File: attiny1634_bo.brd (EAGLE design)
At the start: 49.5 x 22.2 mm, 11 parts, among them J1 AVR_SPI_PRG_6NS, Y1 12MHz

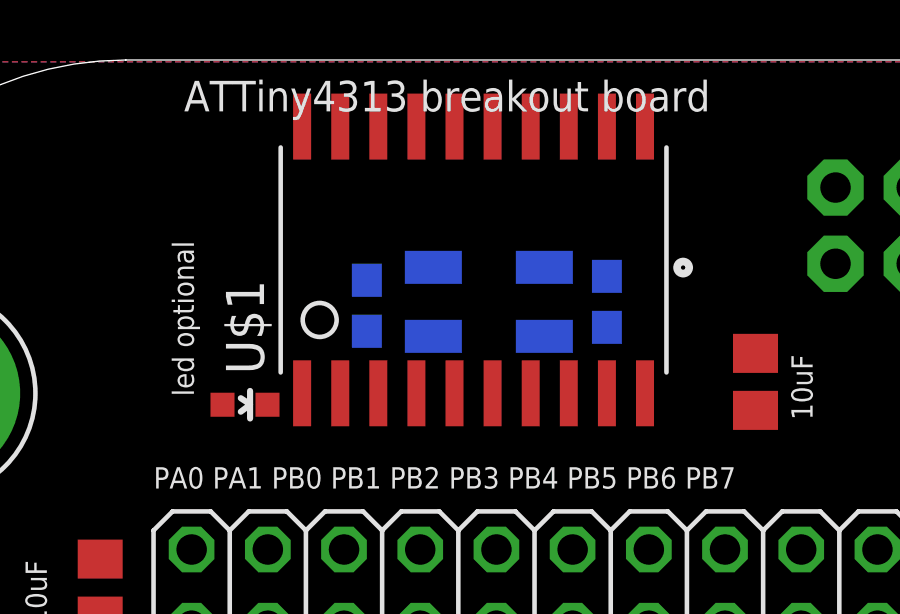
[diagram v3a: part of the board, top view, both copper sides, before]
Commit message: minor fixes to the lib, connected programming signals and xtal
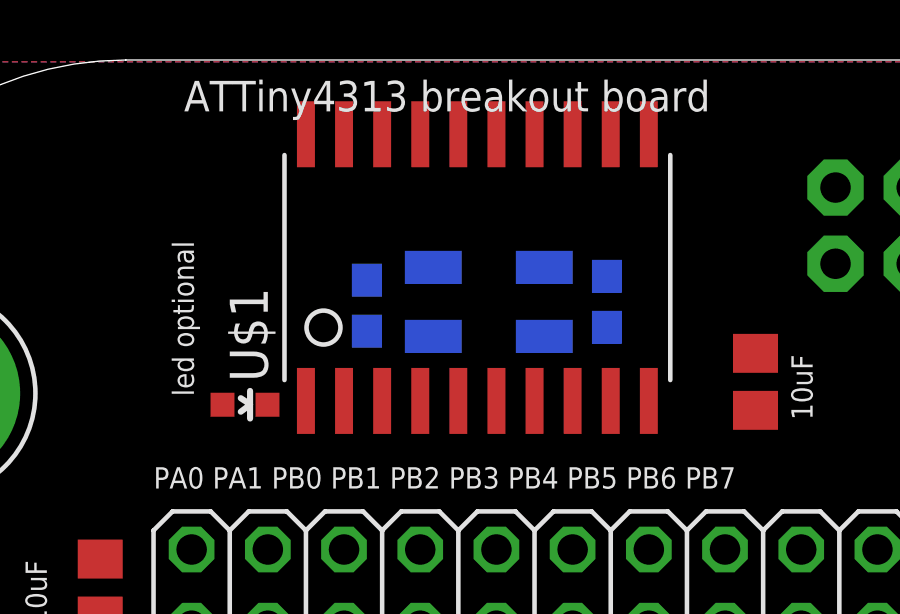
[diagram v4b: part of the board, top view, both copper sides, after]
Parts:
- moved U$1 8.02 mm to (19.3, 15.2)
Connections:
- removed net N$11: CX0.2, Y1.3
- removed net N$3: J1.5
- removed net N$4: J1.4
- removed net N$7: J1.3
- removed net N$9: CX1.2, Y1.1
- removed net PB6/MISO: J1.1
- removed net PD6: LED1.C
- removed net VCC: U$1.11
- new net PB0/MOSI/TX0/ADC5: J1.4, U$1.1
- new net PB1/ADC6: LED1.C, U$1.20
- new net PB2/ADC7/TX1: J1.1, U$1.19
- new net PC1/SCL/ADC10: J1.3, U$1.16
- new net PC3/-RESET: J1.5, U$1.14
- new net PC4/XTAL2: CX0.2, U$1.13, Y1.3
- new net PC5/XTAL1: CX1.2, U$1.12, Y1.1
- net +5V: now also U$1.11
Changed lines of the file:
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@@
 <text x="34.29" y="10.16" size="0.7112" layer="25" font="vector" rot="R90">10uF</text>
 <text x="29.845" y="17.145" size="0.7112" layer="26" rot="MR0">12pF caps for xtal</text>
-<circle x="29.972" y="15.24" radius="0.127" width="0.4064" layer="25"/>
 </plain>
 <attributes>
@@
 <attribute name="VALUE" x="37.719" y="9.017" size="1.27" layer="27" rot="R180"/>
 </element>
-<element name="U$1" library="attiny1634" package="SOIC20" value="ATTINY1634" x="14.097" y="9.144"/>
+<element name="U$1" library="attiny1634" package="SOIC20" value="ATTINY1634" x="19.304" y="15.24"/>
 </elements>
 <signals>
@@
 <contactref element="JP1" pad="18"/>
 <contactref element="U$1" pad="10"/>
+<contactref element="U$1" pad="10"/>
 <wire x1="35.052" y1="15.367" x2="45.466" y2="10.795" width="0" layer="19" extent="1-1"/>
 <wire x1="32.385" y1="12.38" x2="35.052" y2="15.367" width="0" layer="19" extent="1-1"/>
-<wire x1="28.702" y1="11.049" x2="32.385" y2="12.38" width="0" layer="19" extent="1-1"/>
-<wire x1="27.432" y1="14.947" x2="28.702" y2="11.049" width="0" layer="19" extent="1-16"/>
+<wire x1="28.829" y1="10.795" x2="32.385" y2="12.38" width="0" layer="19" extent="1-1"/>
+<wire x1="27.432" y1="14.947" x2="28.829" y2="10.795" width="0" layer="19" extent="1-16"/>
 <wire x1="19.431" y1="13.12" x2="27.432" y2="14.947" width="0" layer="19" extent="16-16"/>
 <wire x1="16.129" y1="3.302" x2="19.431" y2="13.12" width="0" layer="19" extent="16-16"/>
@@
 <contactref element="JP1" pad="2"/>
 <contactref element="JP1" pad="20"/>
+<contactref element="U$1" pad="11"/>
 <wire x1="32.385" y1="10.48" x2="40.132" y2="15.367" width="0" layer="19" extent="1-1"/>
 <wire x1="36.449" y1="3.302" x2="32.385" y2="10.48" width="0" layer="19" extent="1-1"/>
-<wire x1="14.617" y1="10.668" x2="32.385" y2="10.48" width="0" layer="19" extent="1-1"/>
+<wire x1="28.829" y1="19.685" x2="32.385" y2="10.48" width="0" layer="19" extent="1-1"/>
+<wire x1="14.617" y1="10.668" x2="28.829" y2="19.685" width="0" layer="19" extent="1-1"/>
 <wire x1="13.589" y1="3.302" x2="14.617" y2="10.668" width="0" layer="19" extent="1-1"/>
 <wire x1="10.541" y1="3.622" x2="13.589" y2="3.302" width="0" layer="19" extent="1-1"/>
 </signal>
-<signal name="PB6/MISO">
+<signal name="PB1/ADC6">
+<contactref element="LED1" pad="C"/>
+<contactref element="U$1" pad="20"/>
+<wire x1="16.117" y1="10.668" x2="17.399" y2="19.685" width="0" layer="19" extent="1-1"/>
+</signal>
+<signal name="PB0/MOSI/TX0/ADC5">
+<contactref element="J1" pad="4"/>
+<contactref element="U$1" pad="1"/>
+<wire x1="17.399" y1="10.795" x2="37.592" y2="15.367" width="0" layer="19" extent="1-1"/>
+</signal>
+<signal name="PC1/SCL/ADC10">
+<contactref element="U$1" pad="16"/>
+<contactref element="J1" pad="3"/>
+<wire x1="22.479" y1="19.685" x2="37.592" y2="17.907" width="0" layer="19" extent="1-1"/>
+</signal>
+<signal name="PB2/ADC7/TX1">
+<contactref element="U$1" pad="19"/>
 <contactref element="J1" pad="1"/>
-</signal>
-<signal name="PD6">
-<contactref element="LED1" pad="C"/>
-</signal>
-<signal name="N$3">
+<wire x1="18.669" y1="19.685" x2="40.132" y2="17.907" width="0" layer="19" extent="1-1"/>
+</signal>
+<signal name="PC3/-RESET">
+<contactref element="U$1" pad="14"/>
 <contactref element="J1" pad="5"/>
-</signal>
-<signal name="N$4">
-<contactref element="J1" pad="4"/>
-</signal>
-<signal name="N$7">
-<contactref element="J1" pad="3"/>
-</signal>
-<signal name="N$9">
+<wire x1="25.019" y1="19.685" x2="35.052" y2="17.907" width="0" layer="19" extent="1-1"/>
+</signal>
+<signal name="PC5/XTAL1">
+<contactref element="U$1" pad="12"/>
 <contactref element="CX1" pad="2"/>
 <contactref element="Y1" pad="1"/>
+<wire x1="27.432" y1="13.247" x2="27.559" y2="19.685" width="0" layer="19" extent="1-16"/>
 <wire x1="25.345" y1="12.947" x2="27.432" y2="13.247" width="0" layer="19" extent="16-16"/>
 </signal>
-<signal name="N$11">
+<signal name="PC4/XTAL2">
+<contactref element="U$1" pad="13"/>
 <contactref element="CX0" pad="2"/>
 <contactref element="Y1" pad="3"/>
+<wire x1="21.645" y1="15.247" x2="26.289" y2="19.685" width="0" layer="19" extent="1-16"/>
 <wire x1="19.431" y1="14.82" x2="21.645" y2="15.247" width="0" layer="19" extent="16-16"/>
 </signal>
-<signal name="VCC">
-<contactref element="U$1" pad="11"/>
-</signal>
 </signals>

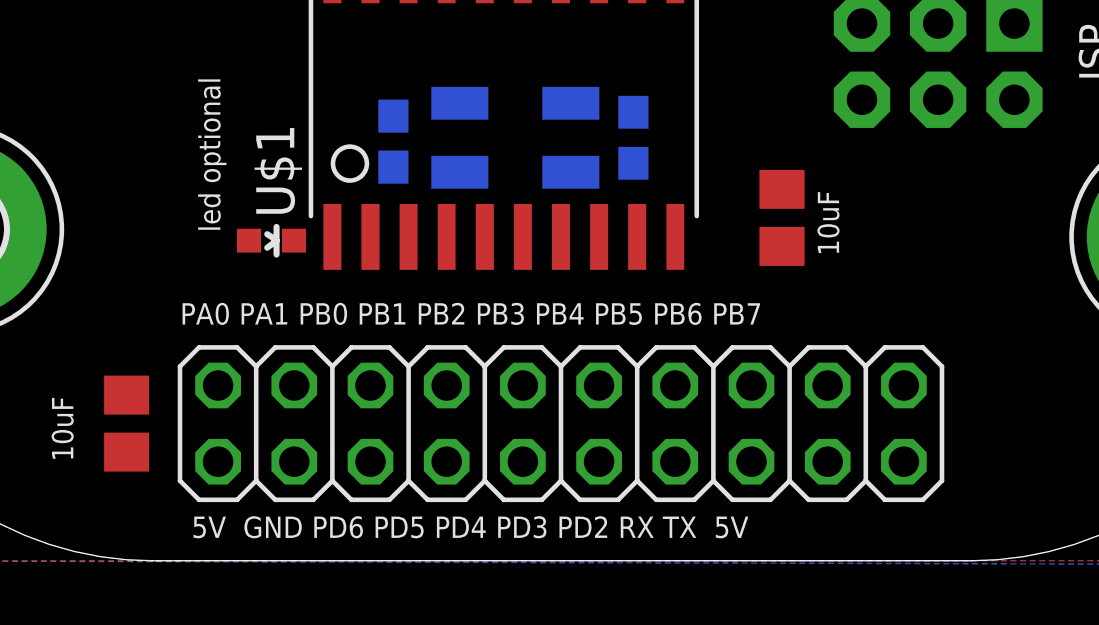
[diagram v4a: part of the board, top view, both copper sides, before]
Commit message: connected portA
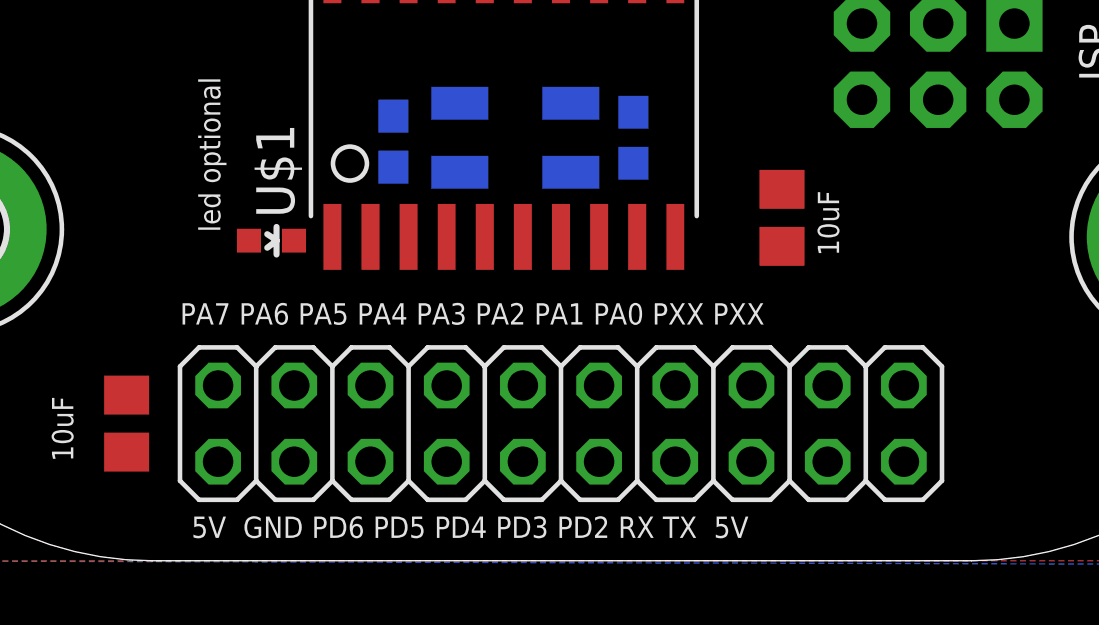
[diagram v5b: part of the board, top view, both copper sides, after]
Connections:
- new net PA0: JP1.5, U$1.9
- new net PA1: JP1.7, U$1.8
- new net PA2: JP1.9, U$1.7
- new net PA3: JP1.11, U$1.6
- new net PA4: JP1.13, U$1.5
- new net PA5: JP1.15, U$1.4
- new net PA6: JP1.17, U$1.3
- new net PA7: JP1.19, U$1.2
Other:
- board text added: "PA7 PA6 PA5 PA4 PA3 PA2 PA1 PA0 PXX PXX"
- board text added: "PXX PXX PA0 PA1 PA2 PA3 PA4 PA5 PA6 PA7"
- board text removed: "PA0 PA1 PB0 PB1 PB2 PB3 PB4 PB5 PB6 PB7"
- board text removed: "PB7 PB6 PB5 PB4 PB3 PB2 PB1 PB0 PA1 PA0"
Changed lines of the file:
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@@
 <text x="13.335" y="20.447" size="1.016" layer="25" font="vector">ATTiny4313 breakout board</text>
 <text x="42.291" y="17.907" size="1.016" layer="25" font="vector" rot="R270">ISP</text>
-<text x="37.338" y="7.874" size="0.7112" layer="26" font="vector" rot="MR0">PB7 PB6 PB5 PB4 PB3 PB2 PB1 PB0 PA1 PA0</text>
+<text x="37.338" y="7.874" size="0.7112" layer="26" font="vector" rot="MR0">PXX PXX PA0 PA1 PA2 PA3 PA4 PA5 PA6 PA7</text>
 <text x="37.211" y="0.635" size="0.762" layer="26" font="vector" rot="MR0">5V RX TX PD2 PD3 PD4 PD5 PD6 GND 5V</text>
-<text x="12.319" y="7.874" size="0.7112" layer="25" font="vector">PA0 PA1 PB0 PB1 PB2 PB3 PB4 PB5 PB6 PB7</text>
+<text x="12.319" y="7.874" size="0.7112" layer="25" font="vector">PA7 PA6 PA5 PA4 PA3 PA2 PA1 PA0 PXX PXX</text>
 <text x="12.7" y="0.762" size="0.7112" layer="25" font="vector">5V  GND PD6 PD5 PD4 PD3 PD2 RX TX  5V</text>
 <text x="28.448" y="18.542" size="0.7112" layer="26" font="vector" rot="MR0">XTAL optional</text>
@@
 <contactref element="U$1" pad="10"/>
 <contactref element="U$1" pad="10"/>
-<wire x1="35.052" y1="15.367" x2="45.466" y2="10.795" width="0" layer="19" extent="1-1"/>
-<wire x1="32.385" y1="12.38" x2="35.052" y2="15.367" width="0" layer="19" extent="1-1"/>
-<wire x1="28.829" y1="10.795" x2="32.385" y2="12.38" width="0" layer="19" extent="1-1"/>
-<wire x1="27.432" y1="14.947" x2="28.829" y2="10.795" width="0" layer="19" extent="1-16"/>
-<wire x1="19.431" y1="13.12" x2="27.432" y2="14.947" width="0" layer="19" extent="16-16"/>
-<wire x1="16.129" y1="3.302" x2="19.431" y2="13.12" width="0" layer="19" extent="16-16"/>
-<wire x1="10.541" y1="5.522" x2="16.129" y2="3.302" width="0" layer="19" extent="1-1"/>
-<wire x1="4.953" y1="11.049" x2="10.541" y2="5.522" width="0" layer="19" extent="1-1"/>
 </signal>
 <signal name="+5V" class="1">
@@
 <wire x1="19.431" y1="14.82" x2="21.645" y2="15.247" width="0" layer="19" extent="16-16"/>
 </signal>
+<signal name="PA0">
+<contactref element="U$1" pad="9"/>
+<contactref element="JP1" pad="5"/>
+<wire x1="31.369" y1="5.842" x2="27.559" y2="10.795" width="0" layer="19" extent="1-1"/>
+</signal>
+<signal name="PA1">
+<contactref element="U$1" pad="8"/>
+<contactref element="JP1" pad="7"/>
+<wire x1="28.829" y1="5.842" x2="26.289" y2="10.795" width="0" layer="19" extent="1-1"/>
+</signal>
+<signal name="PA5">
+<contactref element="JP1" pad="15"/>
+<contactref element="U$1" pad="4"/>
+<wire x1="18.669" y1="5.842" x2="21.209" y2="10.795" width="0" layer="19" extent="1-1"/>
+</signal>
+<signal name="PA4">
+<contactref element="JP1" pad="13"/>
+<contactref element="U$1" pad="5"/>
+<wire x1="21.209" y1="5.842" x2="22.479" y2="10.795" width="0" layer="19" extent="1-1"/>
+</signal>
+<signal name="PA3">
+<contactref element="JP1" pad="11"/>
+<contactref element="U$1" pad="6"/>
+<wire x1="23.749" y1="5.842" x2="23.749" y2="10.795" width="0" layer="19" extent="1-1"/>
+</signal>
+<signal name="PA2">
+<contactref element="JP1" pad="9"/>
+<contactref element="U$1" pad="7"/>
+<wire x1="26.289" y1="5.842" x2="25.019" y2="10.795" width="0" layer="19" extent="1-1"/>
+</signal>
+<signal name="PA7">
+<contactref element="JP1" pad="19"/>
+<contactref element="U$1" pad="2"/>
+<wire x1="13.589" y1="5.842" x2="18.669" y2="10.795" width="0" layer="19" extent="1-1"/>
+</signal>
+<signal name="PA6">
+<contactref element="JP1" pad="17"/>
+<contactref element="U$1" pad="3"/>
+<wire x1="16.129" y1="5.842" x2="19.939" y2="10.795" width="0" layer="19" extent="1-1"/>
+</signal>
 </signals>

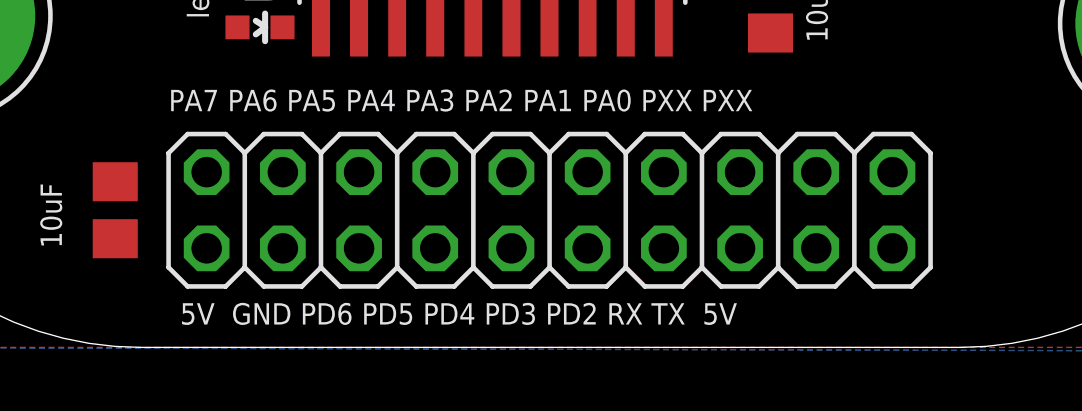
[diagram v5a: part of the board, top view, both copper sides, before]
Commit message: typo fixes, connected portB
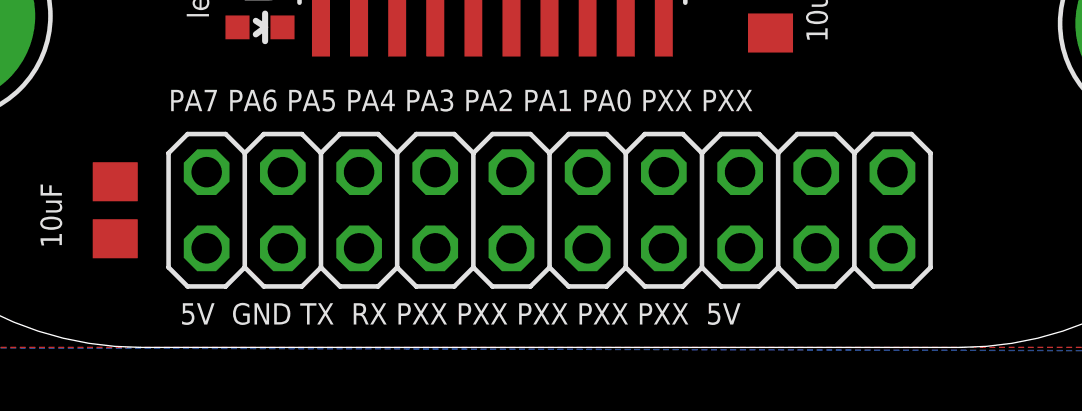
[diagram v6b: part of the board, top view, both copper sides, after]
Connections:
- removed net PB1/ADC6: LED1.C, U$1.20
- new net N$1: JP1.3
- new net N$2: U$1.15
- new net N$4: JP1.6
- new net N$5: JP1.4
- new net N$6: JP1.1
- new net PB1/ADC6/RX1: JP1.14, LED1.C, U$1.20
- new net PB3/ADC8/OC1A: JP1.10, U$1.18
- new net PC0/ADC9/OC0A: JP1.8, U$1.17
- net PB0/MOSI/TX0/ADC5: now also JP1.16
- net PB2/ADC7/TX1: now also JP1.12
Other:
- board text added: "5V GND TX RX PXX PXX PXX PXX PXX 5V"
- board text added: "5V PXX PXX PXX PXX PXX RX TX GND 5V"
- board text removed: "5V GND PD6 PD5 PD4 PD3 PD2 RX TX 5V"
- board text removed: "5V RX TX PD2 PD3 PD4 PD5 PD6 GND 5V"
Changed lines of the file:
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@@
 <text x="42.291" y="17.907" size="1.016" layer="25" font="vector" rot="R270">ISP</text>
 <text x="37.338" y="7.874" size="0.7112" layer="26" font="vector" rot="MR0">PXX PXX PA0 PA1 PA2 PA3 PA4 PA5 PA6 PA7</text>
-<text x="37.211" y="0.635" size="0.762" layer="26" font="vector" rot="MR0">5V RX TX PD2 PD3 PD4 PD5 PD6 GND 5V</text>
+<text x="37.211" y="0.635" size="0.762" layer="26" font="vector" rot="MR0">5V PXX PXX PXX PXX PXX RX TX GND 5V</text>
 <text x="12.319" y="7.874" size="0.7112" layer="25" font="vector">PA7 PA6 PA5 PA4 PA3 PA2 PA1 PA0 PXX PXX</text>
-<text x="12.7" y="0.762" size="0.7112" layer="25" font="vector">5V  GND PD6 PD5 PD4 PD3 PD2 RX TX  5V</text>
+<text x="12.7" y="0.762" size="0.7112" layer="25" font="vector">5V  GND TX  RX PXX PXX PXX PXX PXX  5V</text>
 <text x="28.448" y="18.542" size="0.7112" layer="26" font="vector" rot="MR0">XTAL optional</text>
 <text x="12.954" y="16.129" size="0.7112" layer="25" font="vector" rot="R270">led optional</text>
@@
 <wire x1="10.541" y1="3.622" x2="13.589" y2="3.302" width="0" layer="19" extent="1-1"/>
 </signal>
-<signal name="PB1/ADC6">
+<signal name="PB1/ADC6/RX1">
 <contactref element="LED1" pad="C"/>
 <contactref element="U$1" pad="20"/>
+<contactref element="JP1" pad="14"/>
 <wire x1="16.117" y1="10.668" x2="17.399" y2="19.685" width="0" layer="19" extent="1-1"/>
+<wire x1="21.209" y1="3.302" x2="16.117" y2="10.668" width="0" layer="19" extent="1-1"/>
 </signal>
 <signal name="PB0/MOSI/TX0/ADC5">
 <contactref element="J1" pad="4"/>
 <contactref element="U$1" pad="1"/>
+<contactref element="JP1" pad="16"/>
 <wire x1="17.399" y1="10.795" x2="37.592" y2="15.367" width="0" layer="19" extent="1-1"/>
+<wire x1="18.669" y1="3.302" x2="17.399" y2="10.795" width="0" layer="19" extent="1-1"/>
 </signal>
 <signal name="PC1/SCL/ADC10">
@@
 <contactref element="U$1" pad="19"/>
 <contactref element="J1" pad="1"/>
+<contactref element="JP1" pad="12"/>
 <wire x1="18.669" y1="19.685" x2="40.132" y2="17.907" width="0" layer="19" extent="1-1"/>
+<wire x1="23.749" y1="3.302" x2="18.669" y2="19.685" width="0" layer="19" extent="1-1"/>
 </signal>
 <signal name="PC3/-RESET">
@@
 <wire x1="16.129" y1="5.842" x2="19.939" y2="10.795" width="0" layer="19" extent="1-1"/>
 </signal>
+<signal name="N$4">
+<contactref element="JP1" pad="6"/>
+</signal>
+<signal name="N$5">
+<contactref element="JP1" pad="4"/>
+</signal>
+<signal name="PB3/ADC8/OC1A">
+<contactref element="U$1" pad="18"/>
+<contactref element="JP1" pad="10"/>
+<wire x1="26.289" y1="3.302" x2="19.939" y2="19.685" width="0" layer="19" extent="1-1"/>
+</signal>
+<signal name="PC0/ADC9/OC0A">
+<contactref element="U$1" pad="17"/>
+<contactref element="JP1" pad="8"/>
+<wire x1="28.829" y1="3.302" x2="21.209" y2="19.685" width="0" layer="19" extent="1-1"/>
+</signal>
+<signal name="N$2">
+<contactref element="U$1" pad="15"/>
+</signal>
+<signal name="N$1">
+<contactref element="JP1" pad="3"/>
+</signal>
+<signal name="N$6">
+<contactref element="JP1" pad="1"/>
+</signal>
 </signals>

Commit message: more signals
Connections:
- removed net N$4: JP1.6
- removed net N$5: JP1.4
- net PC4/XTAL2: now also JP1.6
- net PC5/XTAL1: now also JP1.4
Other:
- board text added: "5V GND PB0 PB1 PB2 PB2 PC0 PC4 PC5 5V"
- board text added: "5V PC5 PC3 PC0 PB3 PB2 PB1 PB0 GND 5V"
- board text removed: "5V GND TX RX PXX PXX PXX PXX PXX 5V"
- board text removed: "5V PXX PXX PXX PXX PXX RX TX GND 5V"
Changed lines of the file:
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@@
 <text x="42.291" y="17.907" size="1.016" layer="25" font="vector" rot="R270">ISP</text>
 <text x="37.338" y="7.874" size="0.7112" layer="26" font="vector" rot="MR0">PXX PXX PA0 PA1 PA2 PA3 PA4 PA5 PA6 PA7</text>
-<text x="37.211" y="0.635" size="0.762" layer="26" font="vector" rot="MR0">5V PXX PXX PXX PXX PXX RX TX GND 5V</text>
+<text x="37.211" y="0.635" size="0.7112" layer="26" font="vector" rot="MR0">5V  PC5 PC3 PC0 PB3 PB2 PB1 PB0 GND 5V</text>
 <text x="12.319" y="7.874" size="0.7112" layer="25" font="vector">PA7 PA6 PA5 PA4 PA3 PA2 PA1 PA0 PXX PXX</text>
-<text x="12.7" y="0.762" size="0.7112" layer="25" font="vector">5V  GND TX  RX PXX PXX PXX PXX PXX  5V</text>
+<text x="12.7" y="0.762" size="0.7112" layer="25" font="vector">5V  GND PB0 PB1 PB2 PB2 PC0 PC4 PC5 5V</text>
 <text x="28.448" y="18.542" size="0.7112" layer="26" font="vector" rot="MR0">XTAL optional</text>
 <text x="12.954" y="16.129" size="0.7112" layer="25" font="vector" rot="R270">led optional</text>
@@
 <contactref element="CX1" pad="2"/>
 <contactref element="Y1" pad="1"/>
+<contactref element="JP1" pad="4"/>
 <wire x1="27.432" y1="13.247" x2="27.559" y2="19.685" width="0" layer="19" extent="1-16"/>
 <wire x1="25.345" y1="12.947" x2="27.432" y2="13.247" width="0" layer="19" extent="16-16"/>
+<wire x1="33.909" y1="3.302" x2="27.432" y2="13.247" width="0" layer="19" extent="16-16"/>
 </signal>
 <signal name="PC4/XTAL2">
@@
 <contactref element="CX0" pad="2"/>
 <contactref element="Y1" pad="3"/>
+<contactref element="JP1" pad="6"/>
 <wire x1="21.645" y1="15.247" x2="26.289" y2="19.685" width="0" layer="19" extent="1-16"/>
 <wire x1="19.431" y1="14.82" x2="21.645" y2="15.247" width="0" layer="19" extent="16-16"/>
+<wire x1="31.369" y1="3.302" x2="21.645" y2="15.247" width="0" layer="19" extent="16-16"/>
 </signal>
 <signal name="PA0">
@@
 <wire x1="16.129" y1="5.842" x2="19.939" y2="10.795" width="0" layer="19" extent="1-1"/>
 </signal>
-<signal name="N$4">
-<contactref element="JP1" pad="6"/>
-</signal>
-<signal name="N$5">
-<contactref element="JP1" pad="4"/>
-</signal>
 <signal name="PB3/ADC8/OC1A">
